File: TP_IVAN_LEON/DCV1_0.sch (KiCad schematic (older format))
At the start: 0 parts

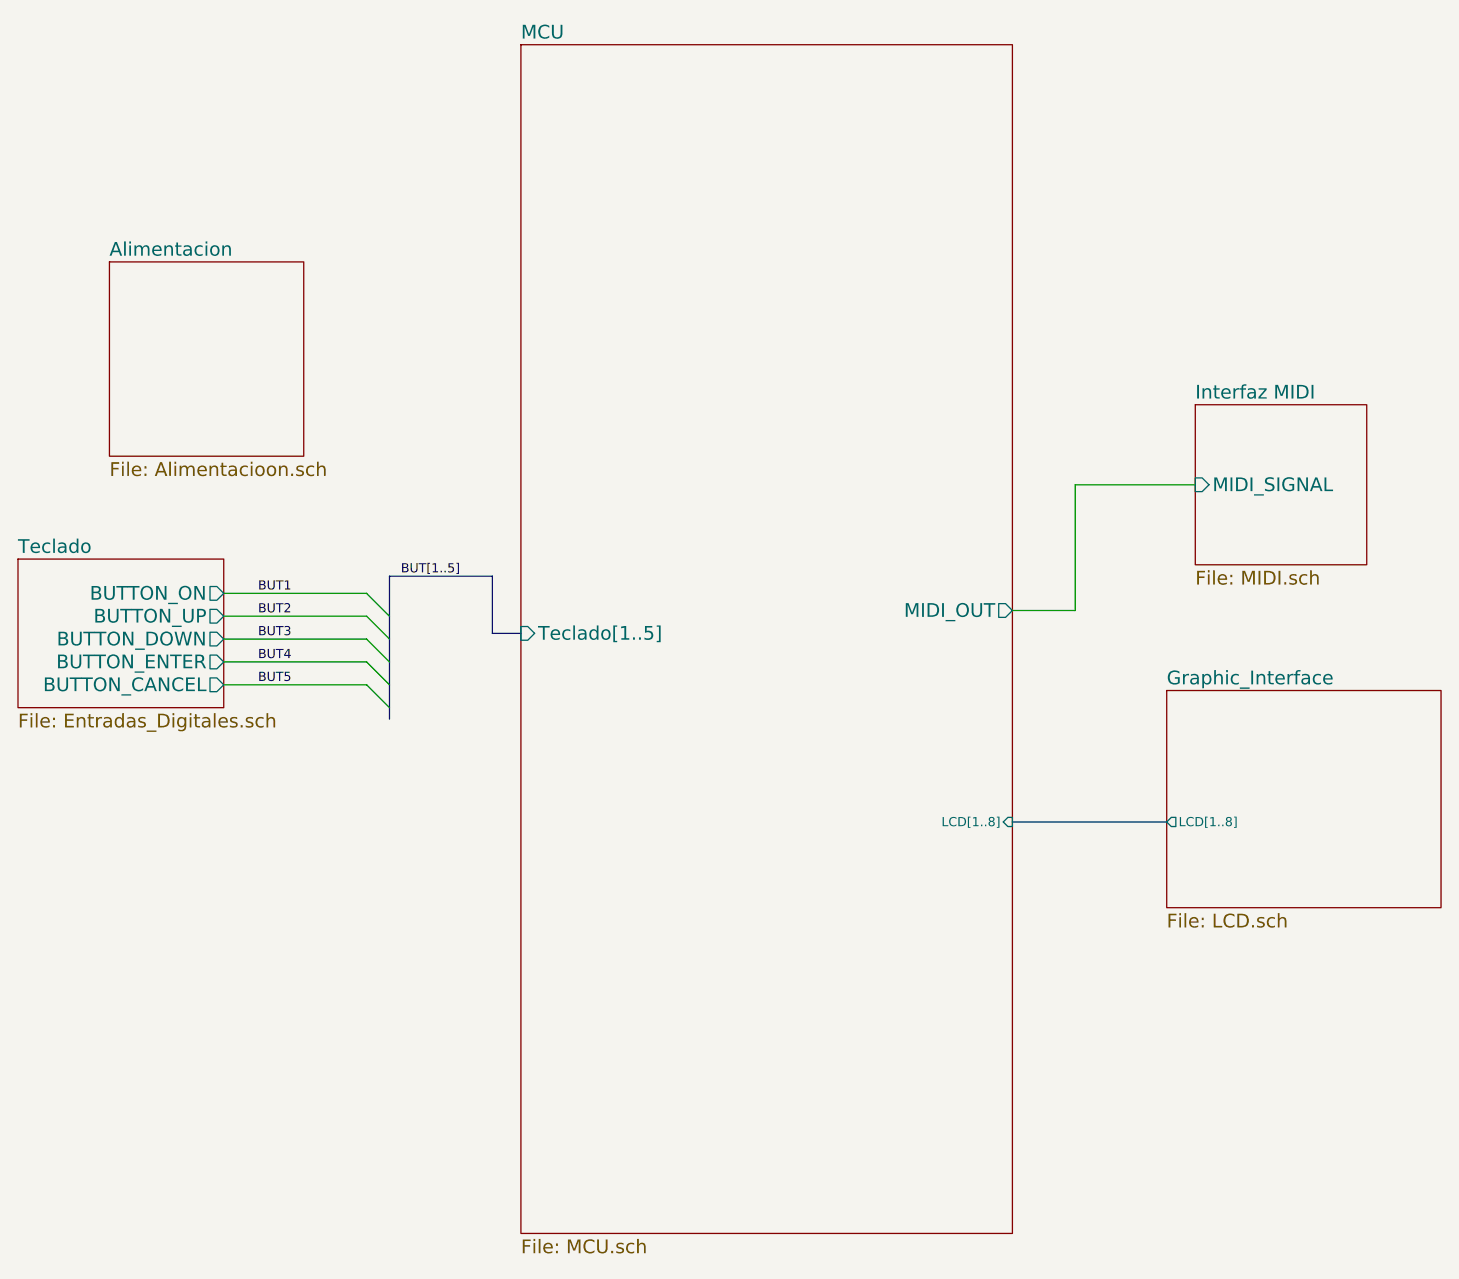
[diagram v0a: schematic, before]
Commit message: Agregado cambios subrayados en verde descritos en documento Leonv.ods en la carpeta docs
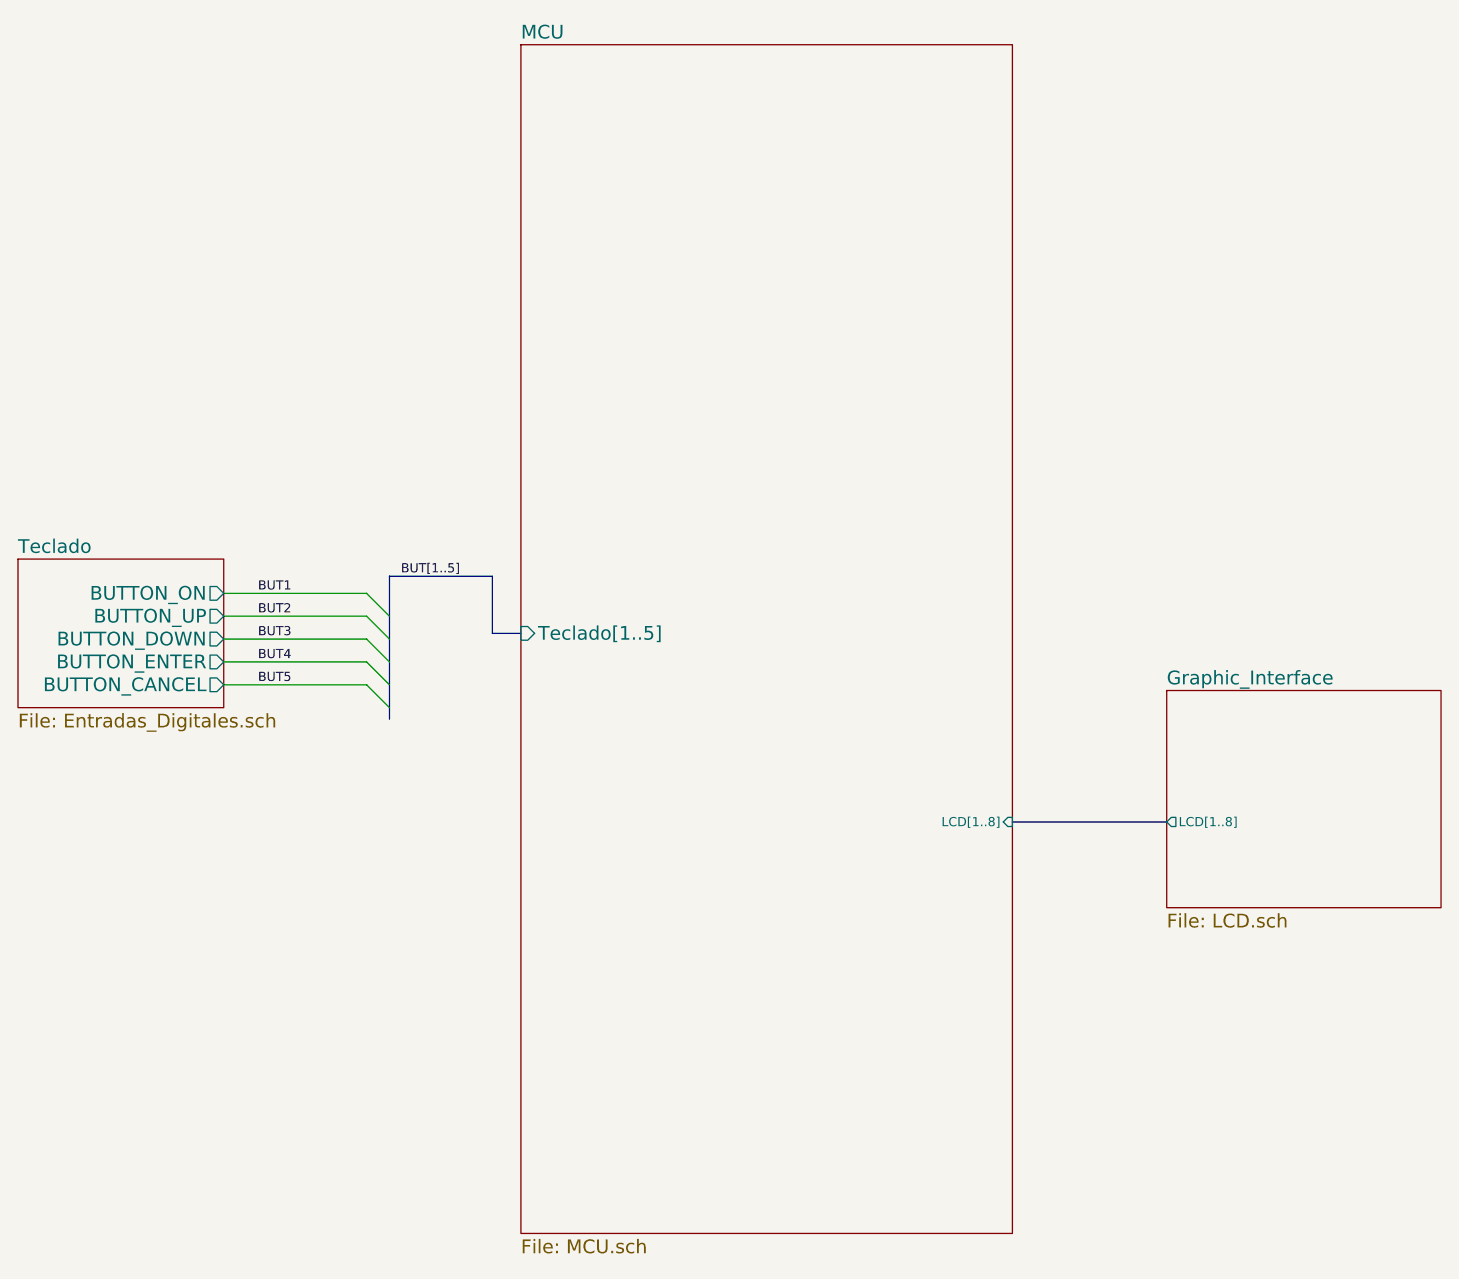
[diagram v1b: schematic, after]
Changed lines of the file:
@@
 $Descr A4 11693 8268
 encoding utf-8
-Sheet 1 6
+Sheet 1 4
 Title "Diagrama Jerarquico"
 Date "12/07/2016"
@@
 $EndDescr
 $Sheet
-S 8200 2475 750  700
-U 5782CA72
-F0 "Interfaz MIDI" 60
-F1 "MIDI.sch" 60
-F2 "MIDI_SIGNAL" I L 8200 2825 60
-$EndSheet
-$Sheet
 S 3050 3150 900  650
 U 5782CAD0
@@
 F5 "BUTTON_ENTER" O R 3950 3600 60
 F6 "BUTTON_CANCEL" O R 3950 3700 60
-$EndSheet
-$Sheet
-S 3450 1850 850  850
-U 5782CAB5
-F0 "Alimentacion" 60
-F1 "Alimentacioon.sch" 60
 $EndSheet
 $Sheet
@@
 F0 "MCU " 60
 F1 "MCU.sch" 60
-F2 "MIDI_OUT" O R 7400 3375 60
-F3 "Teclado[1..5]" I L 5250 3475 60
-F4 "LCD[1..8]" I R 7400 4300 40
+F2 "Teclado[1..5]" I L 5250 3475 60
+F3 "LCD[1..8]" I R 7400 4300 40
 $EndSheet
-Wire Wire Line
-	8200 2825 7675 2825
-Wire Wire Line
-	7675 2825 7675 3375
-Wire Wire Line
-	7675 3375 7400 3375
 Wire Bus Line
 	8075 4300 7400 4300
